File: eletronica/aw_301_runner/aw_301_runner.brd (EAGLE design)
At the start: 50.5 x 50.8 mm, 6 parts, among them IC1 ATTINY2313V

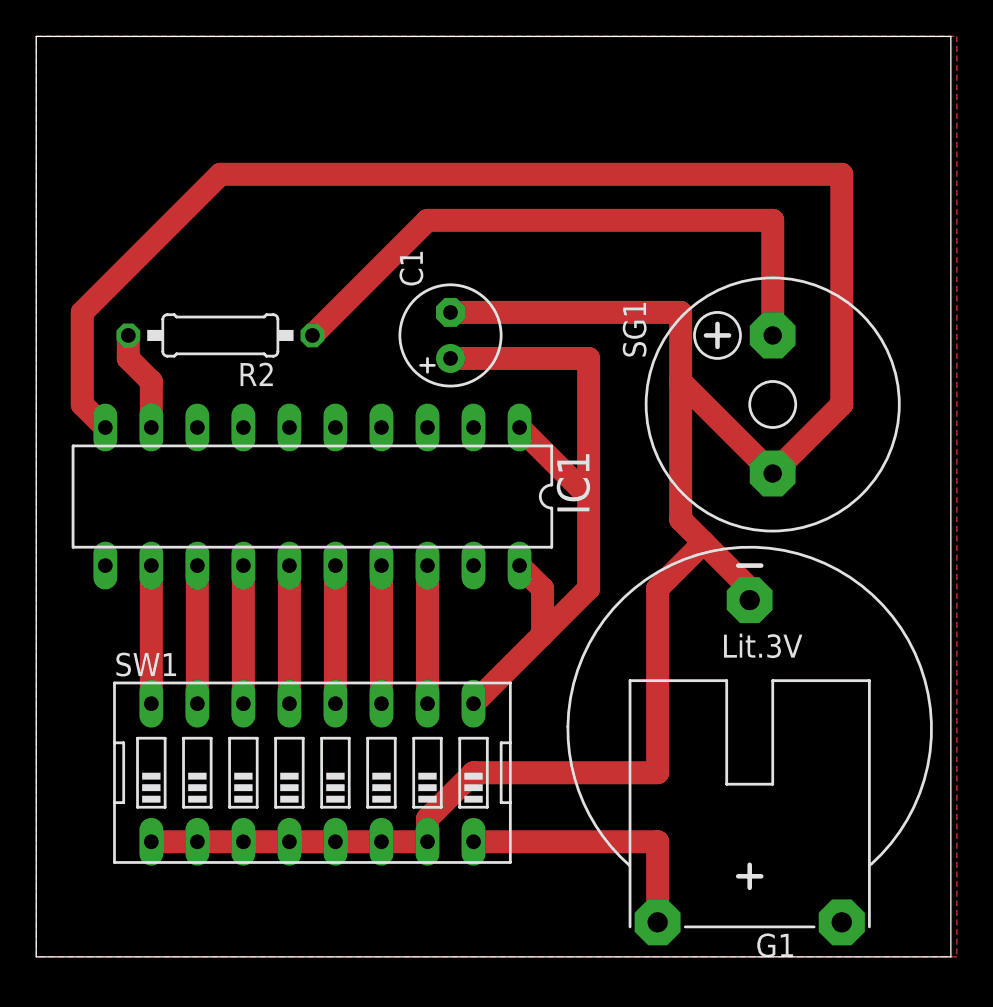
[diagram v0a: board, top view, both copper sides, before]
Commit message: 
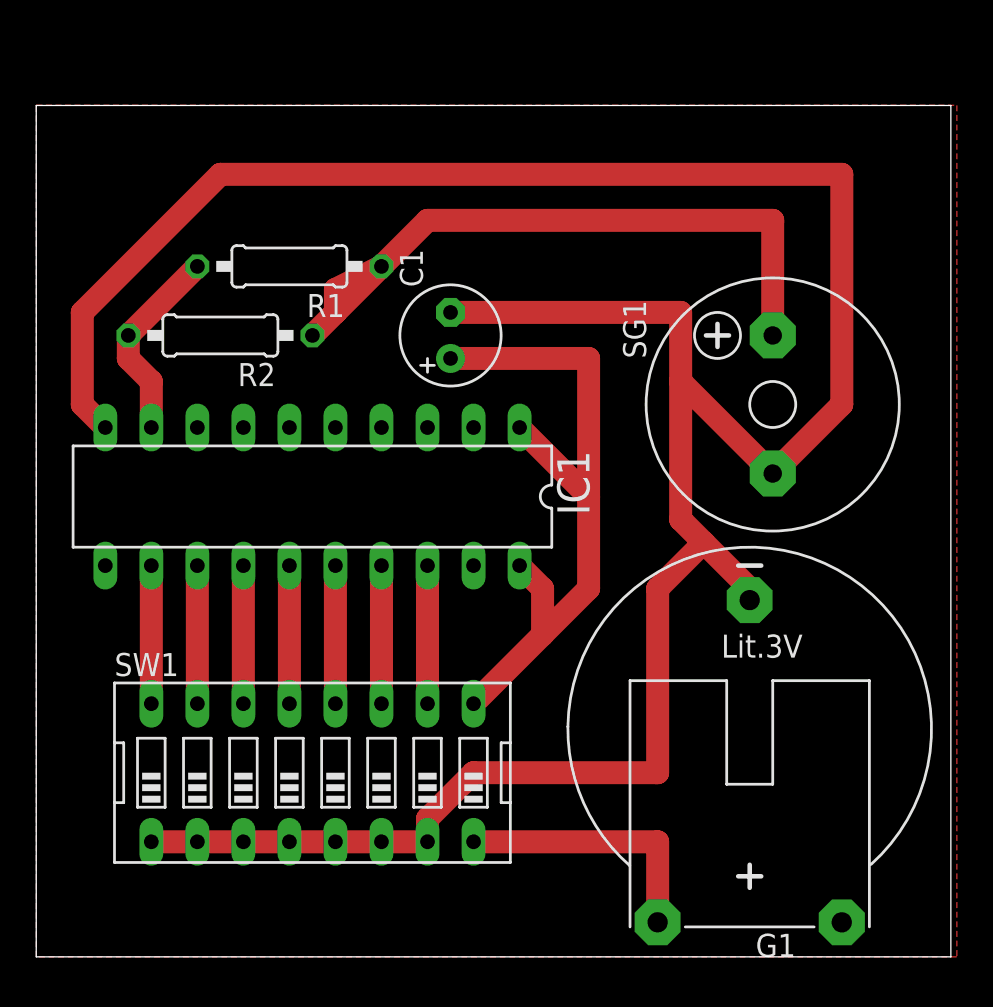
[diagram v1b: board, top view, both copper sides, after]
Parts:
- added R1: 100, rcl:0207/10
- R2: value 50 -> 100
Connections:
- net N$2: now also R1.2
- net N$3: now also R1.1
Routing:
- net N$2: track 5.61 -> 11.0 mm
- net N$3: track 34.4 -> 38.5 mm
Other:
- board size 50.5 x 50.8 mm -> 50.5 x 47 mm
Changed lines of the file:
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@@
 <plain>
 <wire x1="0" y1="0" x2="50.47" y2="0" width="0" layer="20"/>
-<wire x1="50.47" y1="0" x2="50.47" y2="50.79" width="0" layer="20"/>
-<wire x1="50.47" y1="50.79" x2="0" y2="50.79" width="0" layer="20"/>
-<wire x1="0" y1="50.79" x2="0" y2="0" width="0" layer="20"/>
+<wire x1="50.47" y1="0" x2="50.47" y2="46.98" width="0" layer="20"/>
+<wire x1="50.47" y1="46.98" x2="0" y2="46.98" width="0" layer="20"/>
+<wire x1="0" y1="46.98" x2="0" y2="0" width="0" layer="20"/>
 </plain>
 <attributes>
@@
 <element name="G1" library="battery" package="CR2032H" value="CR2032H" x="39.37" y="12.7" rot="R180"/>
 <element name="C1" library="resistor" package="E2,5-6" value="100mF" x="22.86" y="34.29" rot="R90"/>
-<element name="R2" library="rcl" package="0207/10" value="50" x="10.16" y="34.29" rot="R180"/>
+<element name="R2" library="rcl" package="0207/10" value="100" x="10.16" y="34.29" rot="R180"/>
 <element name="SG1" library="buzzer" package="F/CM12P" value="F/CM12P" x="40.64" y="30.48" rot="R90">
 <attribute name="OC_NEWARK" value="unknown" x="40.64" y="30.48" size="1.778" layer="27" rot="R90" display="off"/>
@@
 <attribute name="OC_FARNELL" value="unknown" x="40.64" y="30.48" size="1.778" layer="27" rot="R90" display="off"/>
 </element>
+<element name="R1" library="rcl" package="0207/10" value="100" x="13.97" y="38.1" rot="R180"/>
 </elements>
 <signals>
@@
 <wire x1="5.08" y1="33.02" x2="6.35" y2="31.75" width="1.27" layer="1"/>
 <wire x1="5.08" y1="34.29" x2="5.08" y2="33.02" width="1.27" layer="1"/>
+<contactref element="R1" pad="2"/>
+<wire x1="5.08" y1="34.29" x2="8.89" y2="38.1" width="1.27" layer="1"/>
 </signal>
 <signal name="N$6">
 <polygon width="0.4064" layer="1">
-<vertex x="0" y="50.8"/>
-<vertex x="50.8" y="50.8"/>
+<vertex x="0" y="46.99"/>
+<vertex x="50.8" y="46.99"/>
 <vertex x="50.8" y="0"/>
 <vertex x="0" y="0"/>
@@
 <contactref element="R2" pad="1"/>
 <contactref element="SG1" pad="+"/>
-<wire x1="21.59" y1="40.64" x2="15.24" y2="34.29" width="1.27" layer="1"/>
+<wire x1="21.59" y1="40.64" x2="16.51" y2="35.56" width="1.27" layer="1"/>
+<wire x1="16.51" y1="35.56" x2="15.24" y2="34.29" width="1.27" layer="1"/>
 <wire x1="40.64" y1="40.64" x2="21.59" y2="40.64" width="1.27" layer="1"/>
 <wire x1="40.64" y1="34.29" x2="40.64" y2="40.64" width="1.27" layer="1"/>
+<contactref element="R1" pad="1"/>
+<wire x1="16.51" y1="36.83" x2="19.05" y2="38.1" width="1.27" layer="1"/>
+<wire x1="16.51" y1="35.56" x2="16.51" y2="36.83" width="1.27" layer="1"/>
 </signal>
 <signal name="VCC">

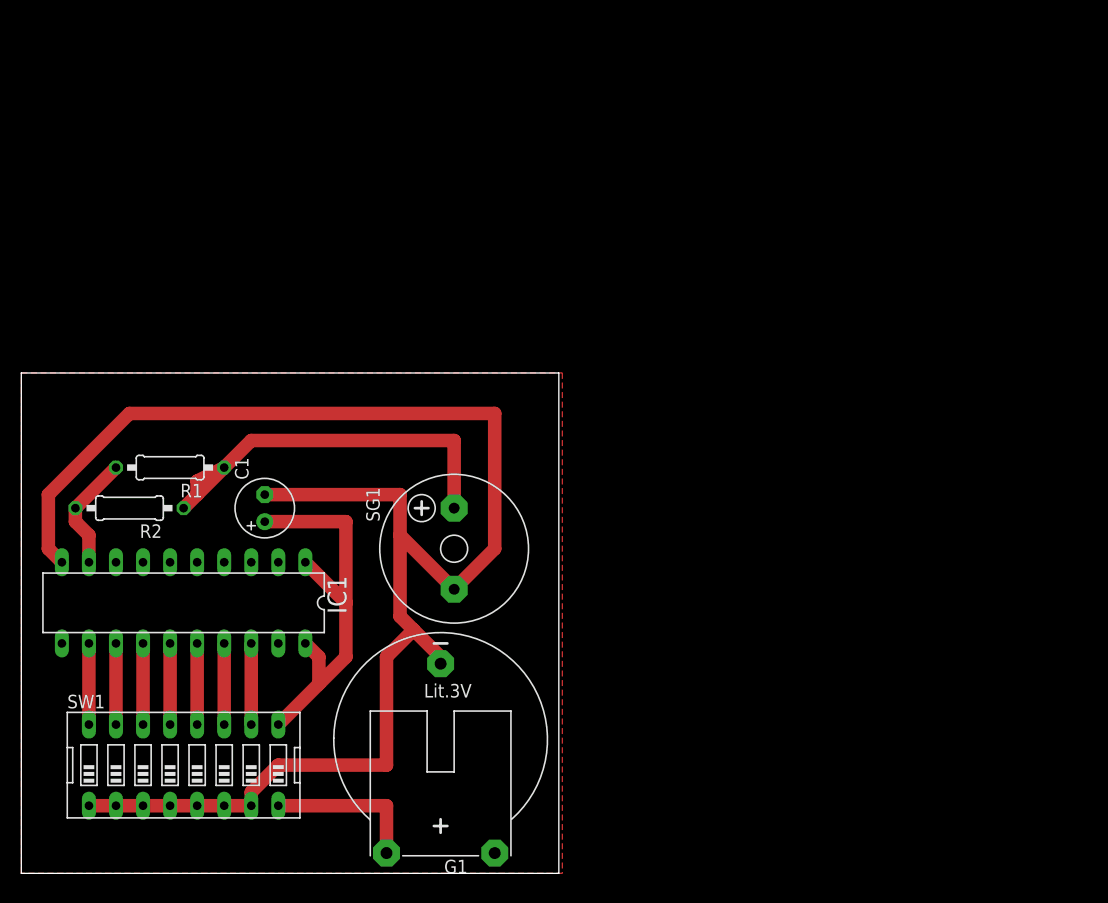
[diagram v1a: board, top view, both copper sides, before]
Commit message: 
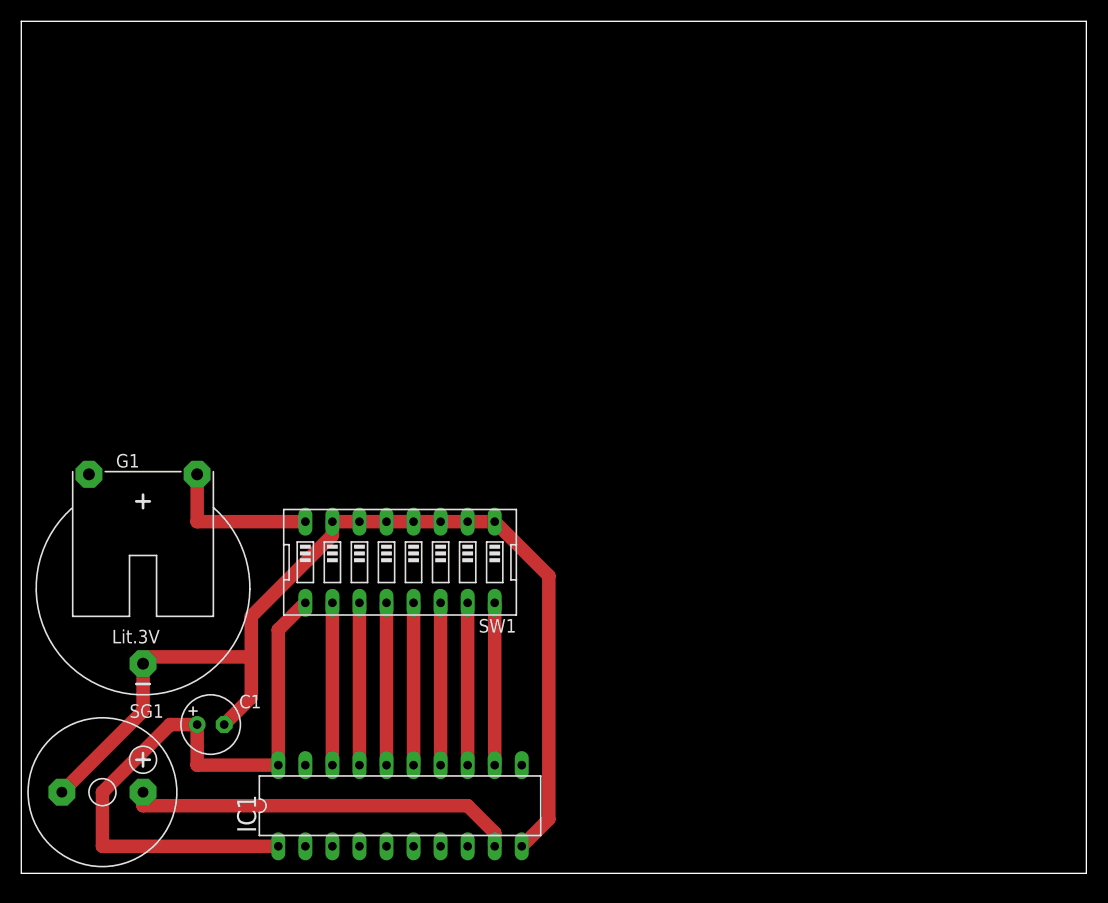
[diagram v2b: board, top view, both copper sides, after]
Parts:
- removed R1, R2: 100, rcl:0207/10
- moved SG1 40.2 mm to (7.62, 7.62), turned to 0 degrees
- moved G1 31.2 mm to (11.4, 26.7), turned to 0 degrees
- moved IC1 27.9 mm to (35.6, 6.35), turned to 0 degrees
- moved SW1 27.9 mm to (35.6, 29.2), turned to 180 degrees
- moved C1 20.9 mm to (17.8, 14.0), turned to 0 degrees
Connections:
- removed net N$2: IC1.9, R1.2, R2.2
- removed net N$3: R1.1, R2.1, SG1.+
- new net N$1: IC1.9, SG1.+
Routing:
- net GND: track 151.4 -> 98.2 mm
- net N$3: track 38.5 -> 0.00 mm
- net N$1: track 0.00 -> 36.6 mm
- net N$5: track 39.0 -> 60.8 mm
- net N$2: track 11.0 -> 0.00 mm
- net N$9: track 7.62 -> 15.2 mm
- net N$8: track 7.62 -> 15.2 mm
- net N$7: track 7.62 -> 15.2 mm
- net N$4: track 7.62 -> 15.2 mm
- net N$12: track 7.62 -> 15.2 mm
- net N$11: track 7.62 -> 15.2 mm
- net N$10: track 7.62 -> 15.2 mm
- removed copper zone on layer 1, net N$6
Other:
- board size 50.5 x 47 mm -> 100 x 80 mm
